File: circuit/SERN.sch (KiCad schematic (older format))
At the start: 43 parts, among them J1 Conn_01x10, J2 Conn_01x02, J3 Conn_01x02, J4 Conn_01x02, J5 Conn_01x01, Q1 Q_NMOS_GDS, T1 12AU7, T4 12AU7

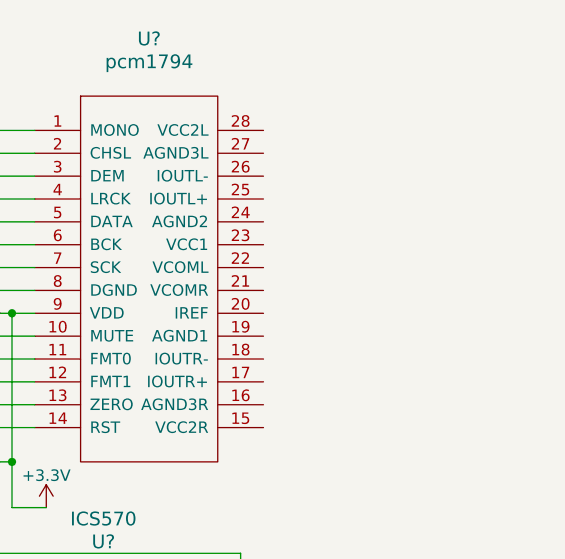
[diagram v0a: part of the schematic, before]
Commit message: [add]アナログ信号周り
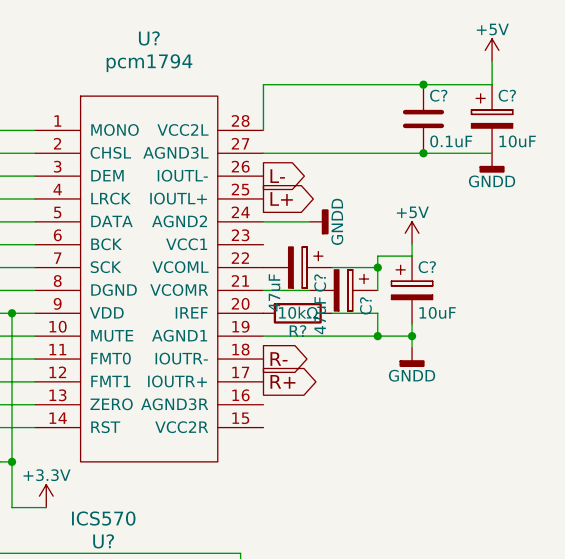
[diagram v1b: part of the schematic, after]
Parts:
- added C?: 0.1uF, symbol C
- added C? (x2): 10uF, symbol CP
- added C? (x2): 47uF, symbol CP
- added R?: 10kΩ, symbol R
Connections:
- net +5V: now also U?.28 (VCC2L), C?.1, C?.1, C?.1, C?.1, C?.1
- net GNDD: now also U?.19 (AGND1), U?.24 (AGND2), U?.27 (AGND3L), C?.2, C?.2, C?.2, R?.1
- net R+: now reaches U?.17 (IOUTR+)
- net R-: now reaches U?.18 (IOUTR-)
- net at U?.20 (IREF): now also R?.2
- net at U?.21 (VCOMR): now also C?.2
- net at U?.22 (VCOML): now also C?.2
- net L+: now reaches U?.25 (IOUTL+)
- net L-: now reaches U?.26 (IOUTL-)
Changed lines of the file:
@@
 	7200 1850 8250 1850
 Connection ~ 9250 3550
+$Comp
+L C C?
+U 1 1 5A3C6654
+P 9950 1200
+F 0 "C?" H 9975 1300 50  0000 L CNN
+F 1 "0.1uF" H 9975 1100 50  0000 L CNN
+F 2 "" H 9988 1050 50  0001 C CNN
+F 3 "" H 9950 1200 50  0001 C CNN
+	1    9950 1200
+	1    0    0    -1
+$EndComp
+$Comp
+L CP C?
+U 1 1 5A3C66D1
+P 10250 1200
+F 0 "C?" H 10275 1300 50  0000 L CNN
+F 1 "10uF" H 10275 1100 50  0000 L CNN
+F 2 "" H 10288 1050 50  0001 C CNN
+F 3 "" H 10250 1200 50  0001 C CNN
+	1    10250 1200
+	1    0    0    -1
+$EndComp
+Wire Wire Line
+	9250 1350 10250 1350
+Connection ~ 9950 1350
+Wire Wire Line
+	9250 1050 9250 1250
+Wire Wire Line
+	9250 1050 10250 1050
+Connection ~ 9950 1050
+$Comp
+L +5V #PWR?
+U 1 1 5A3C6AFF
+P 10250 950
+F 0 "#PWR?" H 10250 800 50  0001 C CNN
+F 1 "+5V" H 10250 1090 50  0000 C CNN
+F 2 "" H 10250 950 50  0001 C CNN
+F 3 "" H 10250 950 50  0001 C CNN
+	1    10250 950
+	1    0    0    -1
+$EndComp
+Wire Wire Line
+	10250 1050 10250 950
+$Comp
+L GNDD #PWR?
+U 1 1 5A3C6C5E
+P 10250 1350
+F 0 "#PWR?" H 10250 1100 50  0001 C CNN
+F 1 "GNDD" H 10250 1225 50  0000 C CNN
+F 2 "" H 10250 1350 50  0001 C CNN
+F 3 "" H 10250 1350 50  0001 C CNN
+	1    10250 1350
+	1    0    0    -1
+$EndComp
+Text GLabel 9250 1450 2    60   Output ~ 0
+L-
+Text GLabel 9250 1550 2    60   Output ~ 0
+L+
+Text GLabel 9250 2250 2    60   Output ~ 0
+R-
+Text GLabel 9250 2350 2    60   Output ~ 0
+R+
+$Comp
+L GNDD #PWR?
+U 1 1 5A3C7828
+P 9450 1650
+F 0 "#PWR?" H 9450 1400 50  0001 C CNN
+F 1 "GNDD" H 9450 1525 50  0000 C CNN
+F 2 "" H 9450 1650 50  0001 C CNN
+F 3 "" H 9450 1650 50  0001 C CNN
+	1    9450 1650
+	0    -1   -1   0
+$EndComp
+Wire Wire Line
+	9250 1650 9450 1650
+$Comp
+L CP C?
+U 1 1 5A3C79B5
+P 9400 1850
+F 0 "C?" H 9425 1950 50  0000 L CNN
+F 1 "47uF" H 9425 1750 50  0000 L CNN
+F 2 "" H 9438 1700 50  0001 C CNN
+F 3 "" H 9400 1850 50  0001 C CNN
+	1    9400 1850
+	0    1    1    0
+$EndComp
+$Comp
+L CP C?
+U 1 1 5A3C7A94
+P 9600 1950
+F 0 "C?" H 9625 2050 50  0000 L CNN
+F 1 "47uF" H 9625 1850 50  0000 L CNN
+F 2 "" H 9638 1800 50  0001 C CNN
+F 3 "" H 9600 1950 50  0001 C CNN
+	1    9600 1950
+	0    1    1    0
+$EndComp
+Wire Wire Line
+	9250 1950 9450 1950
+$Comp
+L +5V #PWR?
+U 1 1 5A3C7C80
+P 9900 1750
+F 0 "#PWR?" H 9900 1600 50  0001 C CNN
+F 1 "+5V" H 9900 1890 50  0000 C CNN
+F 2 "" H 9900 1750 50  0001 C CNN
+F 3 "" H 9900 1750 50  0001 C CNN
+	1    9900 1750
+	1    0    0    -1
+$EndComp
+$Comp
+L GNDD #PWR?
+U 1 1 5A3C7D21
+P 9900 2200
+F 0 "#PWR?" H 9900 1950 50  0001 C CNN
+F 1 "GNDD" H 9900 2075 50  0000 C CNN
+F 2 "" H 9900 2200 50  0001 C CNN
+F 3 "" H 9900 2200 50  0001 C CNN
+	1    9900 2200
+	1    0    0    -1
+$EndComp
+Wire Wire Line
+	9250 2150 9900 2150
+Wire Wire Line
+	9900 2100 9900 2200
+$Comp
+L CP C?
+U 1 1 5A3C7E89
+P 9900 1950
+F 0 "C?" H 9925 2050 50  0000 L CNN
+F 1 "10uF" H 9925 1850 50  0000 L CNN
+F 2 "" H 9938 1800 50  0001 C CNN
+F 3 "" H 9900 1950 50  0001 C CNN
+	1    9900 1950
+	1    0    0    -1
+$EndComp
+Wire Wire Line
+	9900 1800 9900 1750
+Connection ~ 9900 2150
+Wire Wire Line
+	9550 1850 9750 1850
+Wire Wire Line
+	9750 1800 9750 1950
+Wire Wire Line
+	9750 1800 9900 1800
+Connection ~ 9750 1850
+$Comp
+L R R?
+U 1 1 5A3C8307
+P 9400 2050
+F 0 "R?" V 9480 2050 50  0000 C CNN
+F 1 "10kΩ" V 9400 2050 50  0000 C CNN
+F 2 "" V 9330 2050 50  0001 C CNN
+F 3 "" H 9400 2050 50  0001 C CNN
+	1    9400 2050
+	0    1    1    0
+$EndComp
+Wire Wire Line
+	9550 2050 9750 2050
+Wire Wire Line
+	9750 2050 9750 2150
+Connection ~ 9750 2150
 $EndSCHEMATC

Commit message: [update]できた
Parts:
- removed J1: Conn_01x10, Pin_Headers:Pin_Header_Straight_1x10_Pitch2.54mm, symbol Conn_01x10
- added C? (x15): 0.1uF, symbol C
- added C?: 10uF, symbol CP
- added C? (x4): 22pF, symbol C
- added C? (x4): 2200pF, symbol C
- added C? (x4): 2700pF, symbol C
- added C? (x2): 33pF, symbol C
- added J?: Conn_01x16, symbol Conn_01x16
- added J?: Conn_01x03, symbol Conn_01x03
- added R? (x4): 750Ω, symbol R
- added R? (x4): 560Ω, symbol R
- added R? (x4): 270Ω, symbol R
- added R? (x2): 100Ω, symbol R
- added R?: R, symbol R
- added RV?: POT, symbol POT
- added U? (x4): NE5534, symbol NE5534
- added U? (x2): LT1028, symbol NE5534
- added U?: MCW03, symbol MCW03
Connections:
- net +3V3: now also J?.2 (Pin_2), J?.8 (Pin_8), J?.3 (Pin_3), R?.1; no longer J?.1 (Pin_1)
- net +5V: now also J?.1 (Pin_1), U?.15 (VCC2R), U?.23 (VCC1), C?.1, C?.2, J?.16 (Pin_16), J?.2 (Pin_2), RV?.3, U?.2 (+Vin); no longer J?.2 (Pin_2)
- net GNDA: now also C?.2, C?.2, C?.2, C?.2, C?.2, J?.1 (Pin_1), J?.40 (Pin_40), R?.1, U?.1 (MONO), U?.1 (S1), U?.11 (FMT0), U?.12 (FMT1), U?.13 (ZERO), U?.14 (RST), U?.16 (AGND3R), U?.19 (AGND1), U?.2 (CHSL), U?.24 (AGND2), U?.27 (AGND3L), U?.3 (GND), U?.8 (DGND), C?.1, C?.2, C?.2, C?.2, C?.2, C?.2, C?.2, C?.2, C?.2, C?.2, C?.2, C?.2, C?.2, C?.2, C?.2, C?.2, J?.1 (Pin_1), J?.1 (Pin_1), J?.15 (Pin_15), J?.5 (Pin_5), R?.2, R?.2, RV?.1, U?.1 (-Vin), U?.3 (+), U?.3 (+), U?.3 (+), U?.3 (+), U?.3 (On/Off)
- net L+: now also C?.2, R?.2, U?.2 (-)
- net L-: now also C?.2, R?.2, U?.2 (-)
- net Lin: now also R?.1
- net R+: now also C?.2, R?.2, U?.2 (-)
- net R-: now also C?.2, R?.2, U?.2 (-)
- net Rin: now also R?.1
- net at U?.10 (MUTE): now also J?.21 (Pin_21); no longer J?.22 (Pin_22)
- net at U?.4 (LRCK): now also J?.36 (Pin_36); no longer J?.35 (Pin_35)
- net at U?.5 (DATA): now also J?.39 (Pin_39); no longer J?.40 (Pin_40)
- net at U?.4 (ICLK), U?.6 (BCK): now also J?.11 (Pin_11); no longer J?.12 (Pin_12)
- net RS: now reaches J?.16 (Pin_16)
- net RS: now also J?.4 (Pin_4)
- net D4: now reaches J?.30 (Pin_30)
- net D4: now also J?.11 (Pin_11)
- net D7: now reaches J?.31 (Pin_31)
- net D7: now also J?.14 (Pin_14)
- net D5: now reaches J?.32 (Pin_32)
- net D5: now also J?.12 (Pin_12)
- net D6: now reaches J?.34 (Pin_34)
- net D6: now also J?.13 (Pin_13)
- net E: now reaches J?.38 (Pin_38)
- net E: now also J?.6 (Pin_6)
- removed net GNDD: C?.2, C?.2, C?.2, C?.2, C?.2, J?.1 (Pin_1), J?.39 (Pin_39), R?.1, U?.1 (MONO), U?.1 (S1), U?.11 (FMT0), U?.12 (FMT1), U?.13 (ZERO), U?.14 (RST), U?.19 (AGND1), U?.2 (CHSL), U?.24 (AGND2), U?.27 (AGND3L), U?.3 (GND), U?.8 (DGND)
- new net: C?.2, U?.5 (x6)
- new net: C?.1, R?.1, R?.2, U?.6 (x4)
- new net: C?.1, U?.8 (x4)
- new net: C?.2, R?.1, R?.2, U?.2 (-) (x2)
- new net: C?.1, R?.1, R?.1, U?.3 (+) (x2)
- new net: C?.1, C?.1, R?.1, R?.2, U?.6 (x2)
- new net: C?.1, C?.2, U?.7 (common)
- new net: J?.3 (Pin_3), RV?.2
- new net: J?.2 (Pin_2), R?.2
- new net VCC: C?.1, C?.1, C?.1, C?.1, C?.1, C?.1, C?.2, U?.6 (+Vout), U?.7 (V+), U?.7 (V+), U?.7 (V+), U?.7 (V+), U?.7 (V+), U?.7 (V+)
- new net VEE: C?.1, C?.1, C?.1, C?.1, C?.1, C?.1, C?.1, U?.4 (V-), U?.4 (V-), U?.4 (V-), U?.4 (V-), U?.4 (V-), U?.4 (V-), U?.8 (-Vout)
- no-connect marks 14 -> 19
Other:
- moved on the sheet: C1, C2, C3, C4, C5, C6, C?, D2, D3, D4, D5, D6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

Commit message: [completed]DAC基板できたけどLibraryの依存解決できてないのであとでやる（やるとは言ってない）
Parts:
- removed C1, C4, C6: 100uF, Capacitors_THT:CP_Radial_D30.0mm_P10.00mm_SnapIn, symbol CP
- removed C2, C3: 1000uF, Capacitors_THT:CP_Radial_D13.0mm_P5.00mm, symbol CP
- removed C5: 47uF, Capacitors_THT:CP_Radial_D16.0mm_P7.50mm, symbol CP
- removed D2, D3, D4, D5, D6: 1N4007, Diodes_THT:D_T-1_P10.16mm_Horizontal, symbol D
- removed J2, J3, J4: Conn_01x02, Pin_Headers:Pin_Header_Straight_1x02_Pitch2.54mm, symbol Conn_01x02
- removed J5: Conn_01x01, Pin_Headers:Pin_Header_Straight_1x01_Pitch2.54mm, symbol Conn_01x01
- removed J?: Conn_01x16, symbol Conn_01x16
- removed Q1: Q_NMOS_GDS, TO_SOT_Packages_THT:TO-220-3_Vertical, symbol Q_NMOS_GDS
- removed R10, R8: 51, Resistors_THT:R_Axial_DIN0207_L6.3mm_D2.5mm_P10.16mm_Horizontal, symbol R
- removed R11, R12: 100k, Resistors_THT:R_Axial_DIN0414_L11.9mm_D4.5mm_P20.32mm_Horizontal, symbol R
- removed R13: 82k, Resistors_THT:R_Axial_DIN0411_L9.9mm_D3.6mm_P15.24mm_Horizontal, symbol R
- removed R14: 1.5M, Resistors_THT:R_Axial_DIN0207_L6.3mm_D2.5mm_P10.16mm_Horizontal, symbol R
- removed R15, R16, R5, R6: 3.3k, Resistors_THT:R_Axial_DIN0207_L6.3mm_D2.5mm_P10.16mm_Horizontal, symbol R
- removed R17, R18: 5.6k, Resistors_THT:R_Axial_DIN0516_L15.5mm_D5.0mm_P25.40mm_Horizontal, symbol R
- removed R19: 4.7k, Resistors_THT:R_Axial_DIN0207_L6.3mm_D2.5mm_P10.16mm_Horizontal, symbol R
- removed R20: 680k, Resistors_THT:R_Axial_DIN0309_L9.0mm_D3.2mm_P15.24mm_Horizontal, symbol R
- removed R3, R4: 470k, Resistors_THT:R_Axial_DIN0207_L6.3mm_D2.5mm_P10.16mm_Horizontal, symbol R
- removed R7, R9: 620, Resistors_THT:R_Axial_DIN0207_L6.3mm_D2.5mm_P10.16mm_Horizontal, symbol R
- removed RV?: POT, symbol POT
- removed T1, T4: 12AU7, Pin_Headers:Pin_Header_Straight_1x09_Pitch2.54mm, symbol 12AU7
- added J2: Conn_01x04, Pin_Headers:Pin_Header_Straight_1x04_Pitch2.54mm, symbol Conn_01x04
- added J5: Conn_01x03, Pin_Headers:Pin_Header_Straight_1x03_Pitch2.54mm, symbol Conn_01x03
- C1, C10, C14, C18, C2, C22, C23, C27, C28, C29, C3, C30, C35, C36, C7, C8, C9: renamed from C?; footprint (none) -> Capacitors_THT:C_Disc_D5.0mm_W2.5mm_P5.00mm
- C11, C12, C31, C32: renamed from C?; footprint (none) -> Capacitors_THT:C_Rect_L4.0mm_W2.5mm_P2.50mm
- C13, C16: renamed from C?; footprint (none) -> Capacitors_THT:CP_Radial_D6.3mm_P2.50mm
- C15, C17, C19, C4: renamed from C?; footprint (none) -> Capacitors_THT:CP_Radial_D5.0mm_P2.00mm
- C20, C21, C24, C33, C34, C37: renamed from C?; footprint (none) -> Capacitors_THT:C_Rect_L7.0mm_W3.5mm_P5.00mm
- C25, C26, C5, C6: renamed from C?; footprint (none) -> Capacitors_THT:C_Disc_D6.0mm_W2.5mm_P5.00mm
- J1, J4: renamed from J?; footprint (none) -> Pin_Headers:Pin_Header_Straight_1x03_Pitch2.54mm
- J3: renamed from J?; footprint (none) -> Socket_Strips:Socket_Strip_Straight_2x20_Pitch2.54mm
- R1: renamed from R?; value R -> 4.7k; footprint (none) -> Resistors_THT:R_Axial_DIN0204_L3.6mm_D1.6mm_P7.62mm_Horizontal
- R10, R2, R3, R9: renamed from R?; value 750Ω -> 750; footprint (none) -> Resistors_THT:R_Axial_DIN0204_L3.6mm_D1.6mm_P7.62mm_Horizontal
- R11, R16: renamed from R?; value 100Ω -> 100; footprint (none) -> Resistors_THT:R_Axial_DIN0204_L3.6mm_D1.6mm_P7.62mm_Horizontal
- R12, R13, R5, R6: renamed from R?; value 560Ω -> 560; footprint (none) -> Resistors_THT:R_Axial_DIN0204_L3.6mm_D1.6mm_P7.62mm_Horizontal
- R14, R15, R7, R8: renamed from R?; value 270Ω -> 270; footprint (none) -> Resistors_THT:R_Axial_DIN0204_L3.6mm_D1.6mm_P7.62mm_Horizontal
- R4: renamed from R?; value 10kΩ -> 10k; footprint (none) -> Resistors_THT:R_Axial_DIN0204_L3.6mm_D1.6mm_P7.62mm_Horizontal
- U1: renamed from U?; footprint (none) -> SERN:MCW03
- U2, U3, U4, U6, U7, U8, U9: renamed from U?; footprint (none) -> Housings_DIP:DIP-8_W7.62mm_Socket
- U5: renamed from U?; footprint (none) -> Housings_SSOP:SSOP-28_5.3x10.2mm_Pitch0.65mm
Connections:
- net +3V3: now also J3.1 (Pin_1), J3.7 (Pin_7); no longer J3.2 (Pin_2), J3.8 (Pin_8)
- net +5V: now also J3.2 (Pin_2), J2.2 (Pin_2); no longer J3.1 (Pin_1)
- net Lin: now also J5.1 (Pin_1)
- net Rin: now also J5.2 (Pin_2)
- net at U5.10 (MUTE): now also J3.22 (Pin_22); no longer J3.21 (Pin_21)
- net at U5.4 (LRCK): now also J3.35 (Pin_35); no longer J3.36 (Pin_36)
- net at U5.5 (DATA): now also J3.40 (Pin_40); no longer J3.39 (Pin_39)
- net at U4.4 (ICLK), U5.6 (BCK): now also J3.12 (Pin_12); no longer J3.11 (Pin_11)
- net at J3.3 (Pin_3): now also J2.4 (Pin_4)
- net at J3.5 (Pin_5): now also J2.3 (Pin_3)
- net D4: no longer names the net of J3.30 (Pin_30)
- net D5: no longer names the net of J3.32 (Pin_32)
- net D6: no longer names the net of J3.34 (Pin_34)
- net D7: no longer names the net of J3.31 (Pin_31)
- net E: no longer names the net of J3.38 (Pin_38)
- net GNDA renamed GNDD
- net GNDD: now also J3.39 (Pin_39), J2.1 (Pin_1), J5.3 (Pin_3); no longer J3.40 (Pin_40)
- net RS: no longer names the net of J3.16 (Pin_16)
- no-connect marks 19 -> 38
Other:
- moved on the sheet: C1, C2, U1
